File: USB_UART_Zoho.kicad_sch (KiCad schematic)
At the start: 21 parts, among them J2 Peripherals, J3 USB3_A, J4 VccIo_jumper, U1 FT232RL, U2 USBLC6-2P6

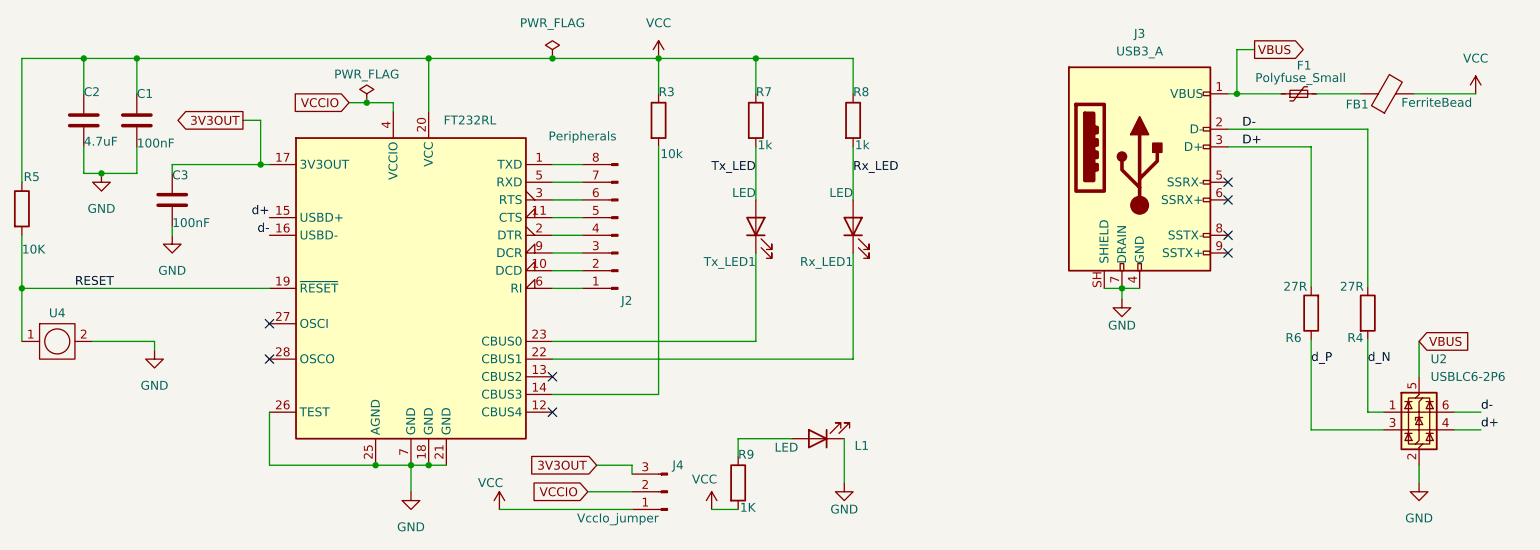
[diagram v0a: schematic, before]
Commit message: major rerouting done: decoupling capacitorsm and resistors placed
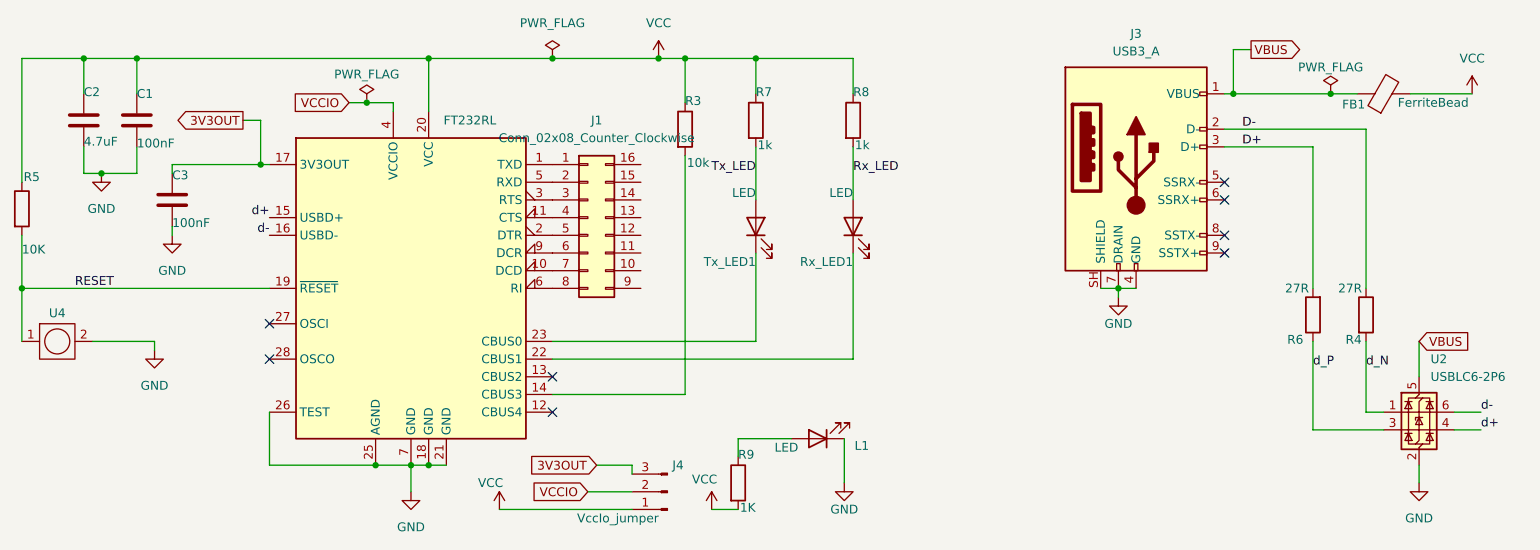
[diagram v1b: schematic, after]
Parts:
- removed F1: Polyfuse_Small, symbol Device:Polyfuse_Small
- removed J2: Peripherals, Connector_PinHeader_2.54mm:PinHeader_1x08_P2.54mm_Horizontal, symbol Connector:Conn_01x08_Pin
- added J1: Conn_02x08_Counter_Clockwise, Connector_PinSocket_2.00mm:PinSocket_2x08_P2.00mm_Horizontal, symbol Connector_Generic:Conn_02x08_Counter_Clockwise
- U4: footprint Button_Switch_THT:SW_PUSH_6mm_H5mm -> Button_Switch_SMD:SW_SPST_TS-1088-xR025
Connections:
- net VBUS: now also FB1.1
- net at U1.1 (TXD): now also J1.1 (Pin_1)
- net at U1.10 (DCD): now also J1.7 (Pin_7)
- net at U1.11 (CTS): now also J1.4 (Pin_4)
- net at U1.2 (DTR): now also J1.5 (Pin_5)
- net at U1.3 (RTS): now also J1.3 (Pin_3)
- net at U1.5 (RXD): now also J1.2 (Pin_2)
- net at U1.6 (RI): now also J1.8 (Pin_8)
- net at U1.9 (DCR): now also J1.6 (Pin_6)
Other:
- moved on the sheet: FB1, J3, R3

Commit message: routing complete: Rev 2/2 09/26
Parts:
- C1, C2, C3: footprint Capacitor_SMD:C_0603_1608Metric_Pad1.08x0.95mm_HandSolder -> Capacitor_SMD:C_0402_1005Metric
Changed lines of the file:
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@@
 			)
 		)
-		(property "Footprint" "Capacitor_SMD:C_0603_1608Metric_Pad1.08x0.95mm_HandSolder"
+		(property "Footprint" "Capacitor_SMD:C_0402_1005Metric"
 			(at 59.3852 80.01 0)
 			(hide yes)
@@
 			)
 		)
-		(property "Footprint" "Capacitor_SMD:C_0603_1608Metric_Pad1.08x0.95mm_HandSolder"
+		(property "Footprint" "Capacitor_SMD:C_0402_1005Metric"
 			(at 51.7652 80.01 0)
 			(hide yes)
@@
 		(in_pos_files yes)
 		(dnp no)
-		(fields_autoplaced yes)
 		(property "Reference" "J1"
-			(at 124.46 76.2 0)
+			(at 124.46 80.01 0)
 			(show_name no)
 			(do_not_autoplace no)
@@
 		(property "Value" "Conn_02x08_Counter_Clockwise"
 			(at 124.46 78.74 0)
+			(hide yes)
 			(show_name no)
 			(do_not_autoplace no)
@@
 			)
 		)
-		(property "Footprint" "Capacitor_SMD:C_0603_1608Metric_Pad1.08x0.95mm_HandSolder"
+		(property "Footprint" "Capacitor_SMD:C_0402_1005Metric"
 			(at 64.4652 91.44 0)
 			(hide yes)
